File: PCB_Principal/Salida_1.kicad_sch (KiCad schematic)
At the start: 41 parts, among them Q61 BC807, Q62 BC559C, Q63 BC549C, Q64 BC549C, Q65 BC559C, Q66 2SD882, Q67 2SB772, U61 LM318

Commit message: Iniciando PCB...
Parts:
- renumbered C61 to C201, C62 to C202, C63 to C203, C64 to C204, C65 to C205, C66 to C206, C67 to C207, D61 to D201, D62 to D202, D63 to D203, D64 to D204, F61 to F201, Q61 to Q201, Q62 to Q202, Q63 to Q203, Q64 to Q204, Q65 to Q205, Q66 to Q206, Q67 to Q207, R61 to R201, R63 to R202, R64 to R203, R62 to R204, R65 to R205, R66 to R206, R67 to R207, R68 to R208, R69 to R209, R70 to R210, R71 to R211, R72 to R212, R73 to R213, R74 to R214, R75 to R215, R76 to R216, R77 to R217, R78 to R218, R79 to R219, R80 to R220, RV61 to RV201, U61 to U201

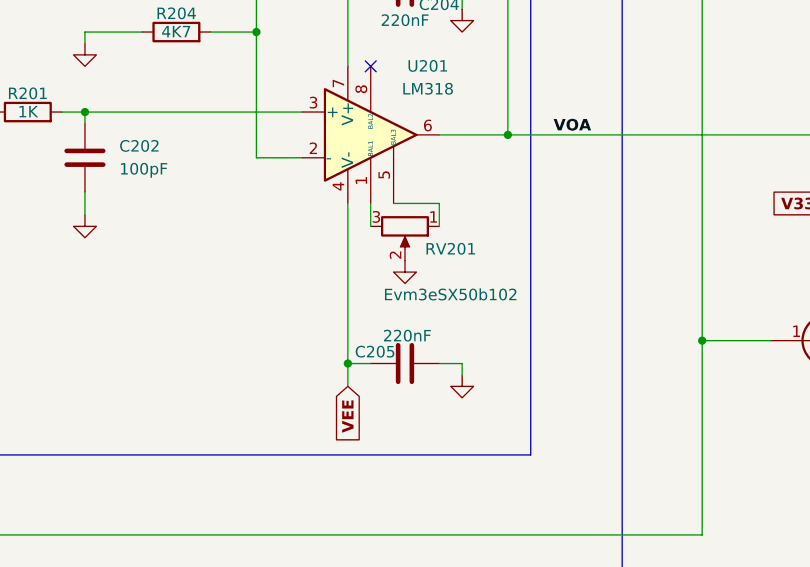
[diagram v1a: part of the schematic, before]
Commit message: Placa con conector J8.
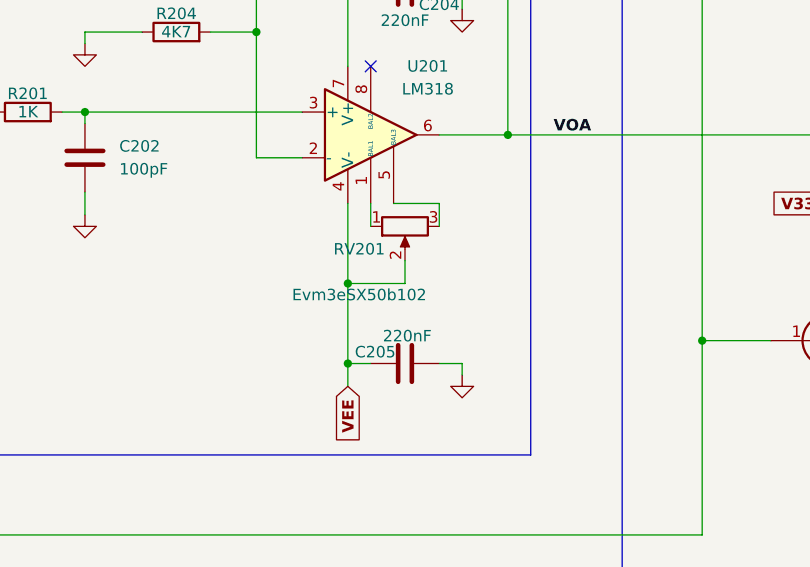
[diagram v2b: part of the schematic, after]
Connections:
- net GND: no longer RV201.2
- net VEE: now also RV201.2
- net at U201.1 (BAL1): now also RV201.1; no longer RV201.3
- net at U201.5 (BAL3): now also RV201.3; no longer RV201.1
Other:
- moved on the sheet: RV201
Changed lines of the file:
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@@
 	)
 	(junction
+		(at 74.93 99.06)
+		(diameter 0)
+		(color 0 0 0 0)
+	)
+	(junction
 		(at 243.84 67.31)
 		(diameter 0)
@@
 	(wire
 		(pts
+			(xy 74.93 99.06) (xy 81.28 99.06)
+		)
+		(stroke
+			(width 0)
+			(type default)
+		)
+	)
+	(wire
+		(pts
 			(xy 217.17 82.55) (xy 217.17 15.24)
 		)
@@
 	(wire
 		(pts
-			(xy 74.93 90.17) (xy 74.93 107.95)
+			(xy 74.93 90.17) (xy 74.93 99.06)
 		)
 		(stroke
@@
 	(wire
 		(pts
+			(xy 74.93 99.06) (xy 74.93 107.95)
+		)
+		(stroke
+			(width 0)
+			(type default)
+		)
+	)
+	(wire
+		(pts
 			(xy 195.58 82.55) (xy 204.47 82.55)
 		)
@@
 	(wire
 		(pts
+			(xy 81.28 96.52) (xy 81.28 99.06)
+		)
+		(stroke
+			(width 0)
+			(type default)
+		)
+	)
+	(wire
+		(pts
 			(xy 85.09 92.71) (xy 85.09 90.17)
 		)
@@
 	)
 	(symbol
-		(lib_id "power:GND")
-		(at 81.28 96.52 0)
-		(unit 1)
-		(exclude_from_sim no)
-		(in_bom yes)
-		(on_board yes)
-		(dnp no)
-		(fields_autoplaced yes)
-		(property "Reference" "#PWR0204"
-			(at 81.28 102.87 0)
-			(effects
-				(font
-					(size 1.27 1.27)
-				)
-				(hide yes)
-			)
-		)
-		(property "Value" "GND"
-			(at 81.28 101.6 0)
-			(effects
-				(font
-					(size 1.27 1.27)
-				)
-				(hide yes)
-			)
-		)
-		(property "Footprint" ""
-			(at 81.28 96.52 0)
-			(effects
-				(font
-					(size 1.27 1.27)
-				)
-				(hide yes)
-			)
-		)
-		(property "Datasheet" ""
-			(at 81.28 96.52 0)
-			(effects
-				(font
-					(size 1.27 1.27)
-				)
-				(hide yes)
-			)
-		)
-		(property "Description" "Power symbol creates a global label with name \"GND\" , ground"
-			(at 81.28 96.52 0)
-			(effects
-				(font
-					(size 1.27 1.27)
-				)
-				(hide yes)
-			)
-		)
-		(pin "1"
-		)
-		(instances
-			(project "ISPEL-CAD_v1"
-				(path "/f66f0001-c0b9-4d2c-a26f-f2bac9dfd594/38615ab2-d421-456a-8594-bd798ea0f00c"
-					(reference "#PWR0204")
-					(unit 1)
-				)
-			)
-		)
-	)
-	(symbol
 		(lib_id "Transistor_BJT:2SD600")
 		(at 193.04 57.15 0)
@@
 	(symbol
 		(lib_id "Device:R_Potentiometer")
-		(at 81.28 92.71 270)
+		(at 81.28 92.71 90)
+		(mirror x)
 		(unit 1)
 		(exclude_from_sim no)
@@
 		(dnp no)
 		(property "Reference" "RV201"
-			(at 86.36 95.25 90)
+			(at 76.2 95.25 90)
 			(effects
 				(font
@@
 		)
 		(property "Value" "Evm3eSX50b102"
-			(at 86.36 100.33 90)
+			(at 76.2 100.33 90)
 			(effects
 				(font

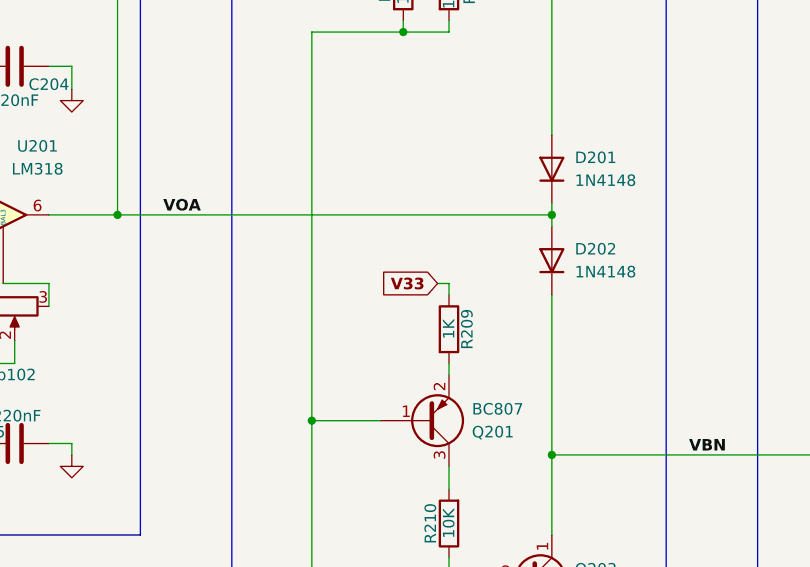
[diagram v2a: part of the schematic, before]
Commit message: Placa PCB con ERC. Falta huella de portafusibles.
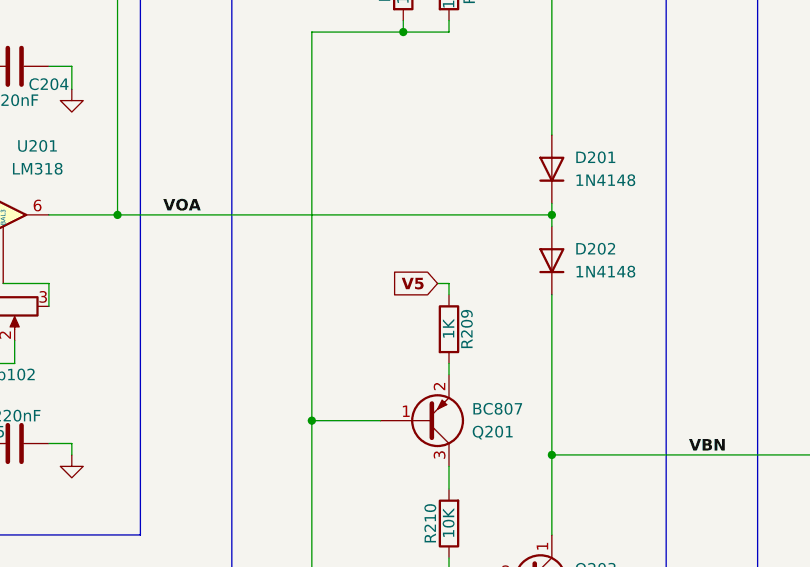
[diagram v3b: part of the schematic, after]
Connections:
- net V33 renamed V5
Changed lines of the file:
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@@
 		)
 	)
-	(global_label "V33"
+	(global_label "V5"
 		(shape input)
 		(at 128.27 90.17 180)
@@
 		)
 		(property "Intersheetrefs" "${INTERSHEET_REFS}"
-			(at 121.3012 90.17 0)
+			(at 122.5107 90.17 0)
 			(effects
 				(font

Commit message: PCB con huella de portafusibles 1808.
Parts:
- F201: footprint Fuse:Fuse_1812_4532Metric_Pad1.30x3.40mm_HandSolder -> Libreria_ISPEL:Fuseholder_1808_handsoldering
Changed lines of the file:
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@@
 			)
 		)
-		(property "Footprint" "Fuse:Fuse_1812_4532Metric_Pad1.30x3.40mm_HandSolder"
+		(property "Footprint" "Libreria_ISPEL:Fuseholder_1808_handsoldering"
 			(at 237.49 84.328 90)
 			(effects

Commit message: Corrigiendo PCB con comentarios AS.
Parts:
- R218, R219: footprint Resistor_THT:R_Axial_DIN0414_L11.9mm_D4.5mm_P5.08mm_Vertical -> Resistor_THT:R_Axial_DIN0414_L11.9mm_D4.5mm_P15.24mm_Horizontal
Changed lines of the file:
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@@
 			)
 		)
-		(property "Footprint" "Resistor_THT:R_Axial_DIN0414_L11.9mm_D4.5mm_P5.08mm_Vertical"
+		(property "Footprint" "Resistor_THT:R_Axial_DIN0414_L11.9mm_D4.5mm_P15.24mm_Horizontal"
 			(at 237.49 69.088 90)
 			(effects
@@
 			)
 		)
-		(property "Footprint" "Resistor_THT:R_Axial_DIN0414_L11.9mm_D4.5mm_P5.08mm_Vertical"
+		(property "Footprint" "Resistor_THT:R_Axial_DIN0414_L11.9mm_D4.5mm_P15.24mm_Horizontal"
 			(at 237.49 72.898 90)
 			(effects

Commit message: Revisión 1. Con prototipo ISPEL Beta 2024 en fase de prueba.
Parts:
- R216, R217: value 1M -> CAL
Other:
- title: Salida 1 (ISPEL Beta 2024) -> Salida 1 (ISPEL Beta)
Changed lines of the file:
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@@
 	(paper "A4")
 	(title_block
-		(title "Salida 1 (ISPEL Beta 2024)")
-		(date "2024-10-29")
-		(rev "2 (GC)")
+		(title "Salida 1 (ISPEL Beta)")
+		(date "2025-04-04")
+		(rev "1")
 	)
 	(junction
@@
 			)
 		)
-		(property "Value" "1M"
+		(property "Value" "CAL"
 			(at 204.47 89.154 90)
 			(effects
@@
 			)
 		)
-		(property "Value" "1M"
+		(property "Value" "CAL"
 			(at 204.47 78.74 90)
 			(effects
